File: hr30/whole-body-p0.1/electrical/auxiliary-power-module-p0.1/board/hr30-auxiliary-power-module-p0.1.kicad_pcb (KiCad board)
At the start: 2 copper layers, 120 x 58 mm, 19 parts, among them U1 REC30E-2405SZ COMPUTE isolate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, U2 REC30E-2405SZ HMI isolated co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, U3 REC30E-2405SZ CONTROL isolate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

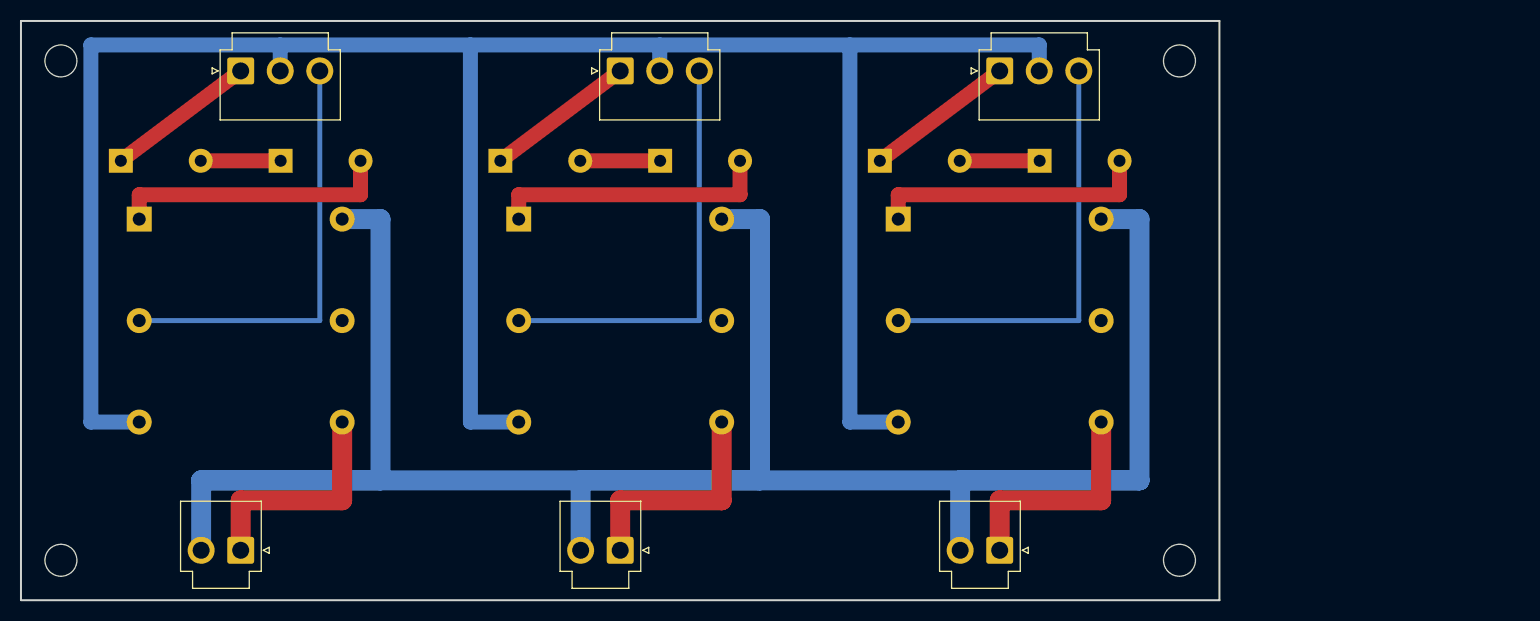
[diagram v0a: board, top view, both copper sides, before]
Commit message: Increase HR-30 HMI power margin
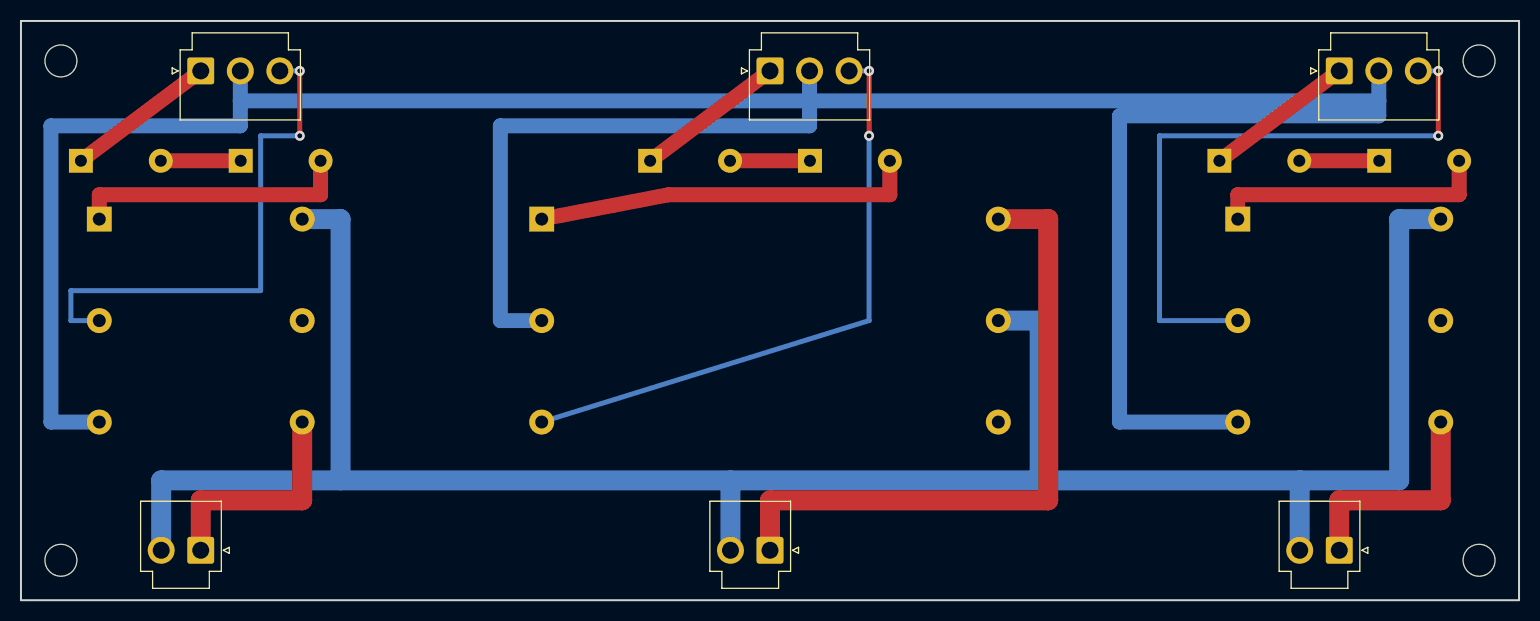
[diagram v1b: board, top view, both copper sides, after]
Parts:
- U2: value REC30E-2405SZ HMI isolated converter -> TEN 40-1211E HMI isolated converter; footprint HR30_AUX:REC30E-Z -> HR30_AUX:TEN40E
- moved F3 34.0 mm to (124.0, 14.0)
- moved JI3 34.0 mm to (132.0, 5.00)
- moved JO3 34.0 mm to (132.0, 53.0)
- moved RP3 34.0 mm to (140.0, 14.0)
- moved U3 34.0 mm to (132.0, 30.0)
- moved H2 30.0 mm to (146.0, 4.00)
- moved H4 30.0 mm to (146.0, 54.0)
- moved F2 15.0 mm to (67.0, 14.0)
- moved JI2 15.0 mm to (75.0, 5.00)
- moved JO2 15.0 mm to (75.0, 53.0)
- moved RP2 15.0 mm to (83.0, 14.0)
- moved U2 15.0 mm to (75.0, 30.0)
- moved F1 4.00 mm to (10.0, 14.0)
- moved JI1 4.00 mm to (18.0, 5.00)
- moved JO1 4.00 mm to (18.0, 53.0)
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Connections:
- U2 pad 4: AUX_0V_STAR -> HMI_5V0
- U2 pad 5: (no net) -> AUX_0V_STAR
- U2 pad 6: HMI_5V0 -> (no net)
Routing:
- net ACT_0V_CONTROLLED: track 230.6 -> 306.0 mm
- net HMI_5V0: track 23.0 -> 66.0 mm
- net AUX_0V_STAR: track 258.8 -> 225.4 mm
- net CONTROL_DISABLE_N: track 43.1 -> 62.8 mm, vias 0 -> 2
- net HMI_DISABLE_N: track 43.1 -> 61.3 mm, vias 0 -> 2
- net HMI_12V_PROTECTED: track 28.0 -> 38.5 mm
- net COMPUTE_DISABLE_N: track 43.1 -> 52.8 mm, vias 0 -> 2
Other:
- board size 120 x 58 mm -> 150 x 58 mm
